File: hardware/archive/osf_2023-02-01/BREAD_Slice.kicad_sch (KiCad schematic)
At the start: 37 parts, among them J1 Conn_01x10_Female, J2 Term_2, J3 Term_2, J4 Term_2, J5 Term_2, J7 Term_2, J8 Term_2, K1 G5Q-1, U1 MCP6001U, U2 MCP6001U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

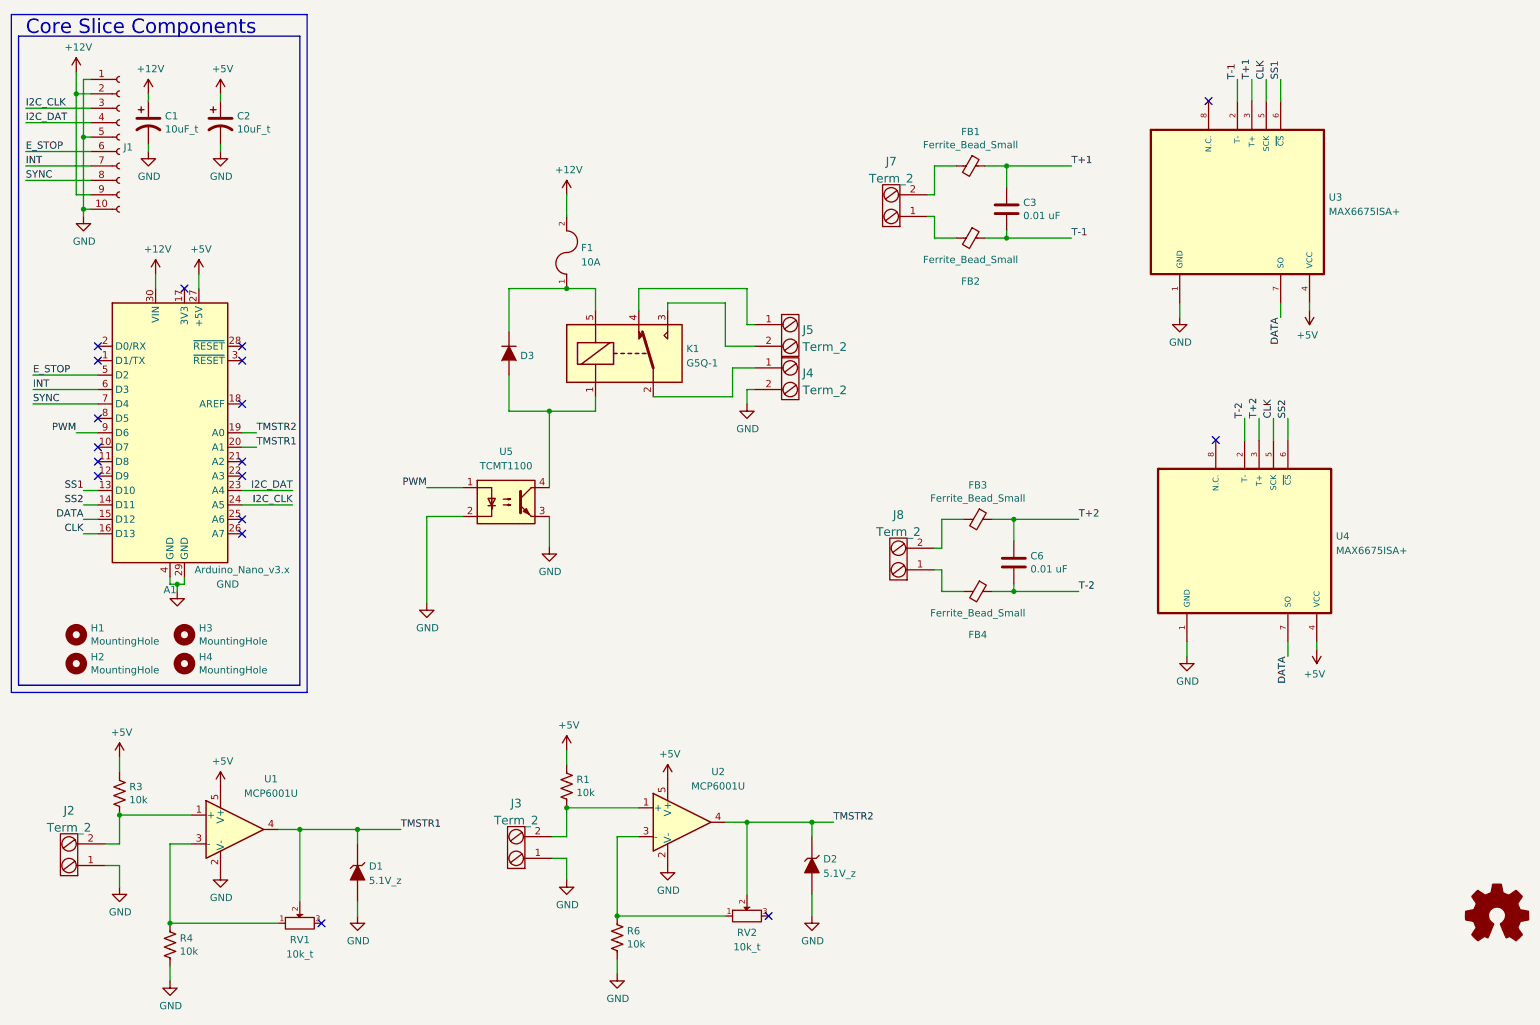
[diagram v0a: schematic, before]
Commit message: added historical scripts and new revisions
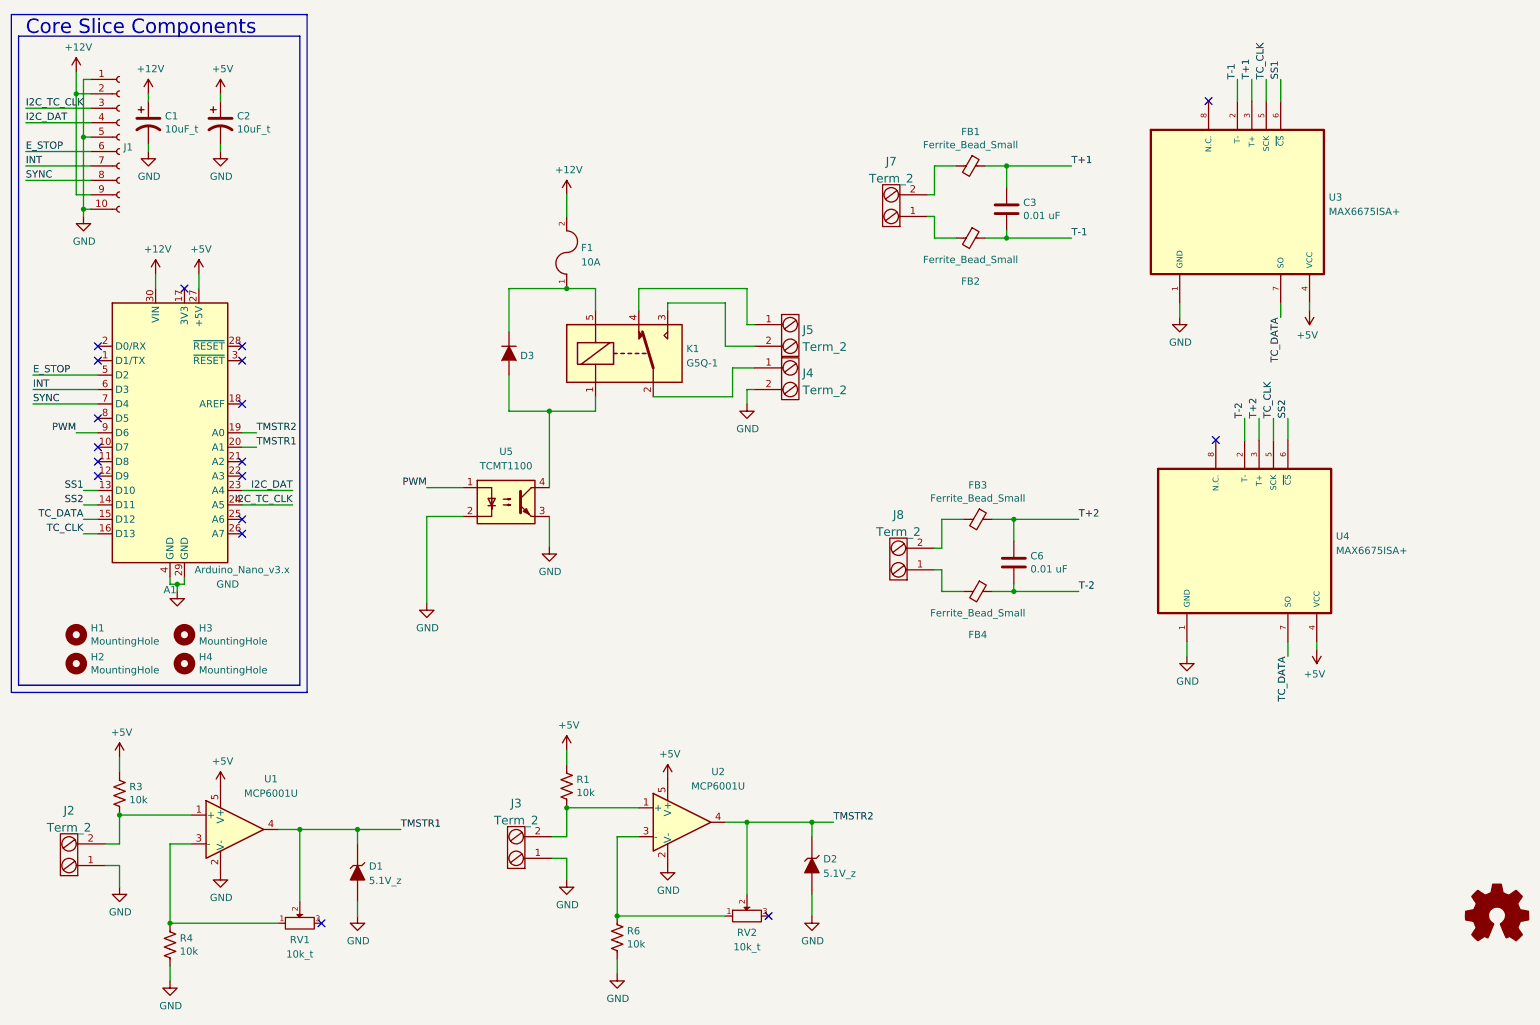
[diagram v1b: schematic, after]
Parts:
- A1: TC_DATAsheet (none) -> http://www.mouser.com/pdfdocs/Gravitech_Arduino_Nano3_0.pdf
- C1, C2: TC_DATAsheet (none) -> https://www.digikey.com/short/qcd8n7
- D1, D2: TC_DATAsheet (none) -> https://www.digikey.com/short/q75wjm
- D3: TC_DATAsheet (none) -> https://www.digikey.com/short/q75wqm
- F1: TC_DATAsheet (none) -> https://www.digikey.com/short/q7wbwz
- J2, J3, J4, J5, J7, J8: TC_DATAsheet (none) -> https://www.digikey.com/short/q7wbhd
- K1: TC_DATAsheet (none) -> https://www.omron.com/ecb/products/pdf/en-g5q.pdf
- RV1, RV2: TC_DATAsheet (none) -> https://www.digikey.com/short/qt5j3q
- U1, U2: TC_DATAsheet (none) -> http://ww1.microchip.com/downloads/en/DeviceDoc/21733j.pdf
- U5: TC_DATAsheet (none) -> http://www.vishay.com/docs/83510/tcmt1100.pdf
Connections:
- net CLK renamed TC_CLK
- net DATA renamed TC_DATA
- net I2C_CLK renamed I2C_TC_CLK
